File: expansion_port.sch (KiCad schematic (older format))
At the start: 2 parts

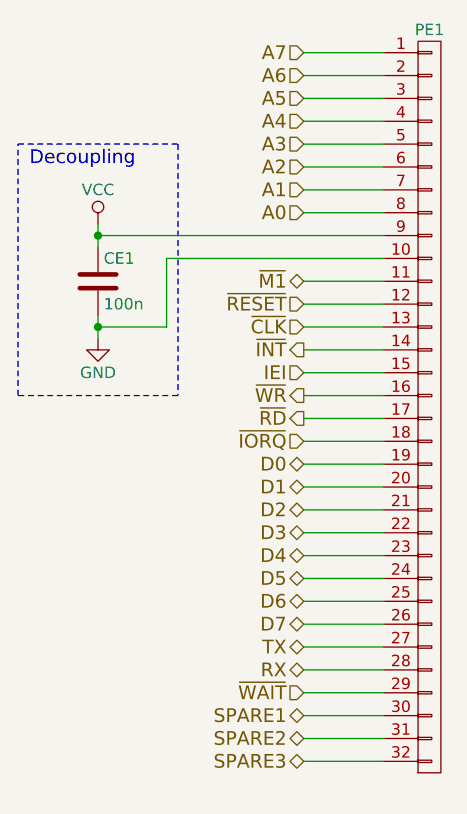
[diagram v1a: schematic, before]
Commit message: Added new expansion and GAL to layout.
Haven't routed the osc. or the reset.
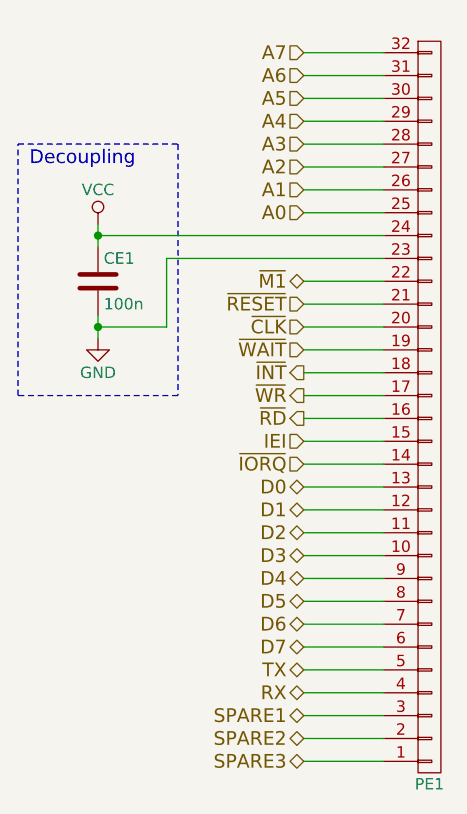
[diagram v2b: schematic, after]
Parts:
- PE1: footprint (none) -> Socket_Strips:Socket_Strip_Angled_1x32
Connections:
- net A0: now also PE1.25 (P25); no longer PE1.8 (P8)
- net A1: now also PE1.26 (P26); no longer PE1.7 (P7)
- net A2: now also PE1.27 (P27); no longer PE1.6 (P6)
- net A3: now also PE1.28 (P28); no longer PE1.5 (P5)
- net A4: now also PE1.29 (P29); no longer PE1.4 (P4)
- net A5: now also PE1.30 (P30); no longer PE1.3 (P3)
- net A6: now also PE1.31 (P31); no longer PE1.2 (P2)
- net A7: now also PE1.32 (P32); no longer PE1.1 (P1)
- net D0: now also PE1.13 (P13); no longer PE1.19 (P19)
- net D1: now also PE1.12 (P12); no longer PE1.20 (P20)
- net D2: now also PE1.11 (P11); no longer PE1.21 (P21)
- net D3: now also PE1.10 (P10); no longer PE1.22 (P22)
- net D4: now also PE1.9 (P9); no longer PE1.23 (P23)
- net D5: now also PE1.8 (P8); no longer PE1.24 (P24)
- net D6: now also PE1.7 (P7); no longer PE1.25 (P25)
- net D7: now also PE1.6 (P6); no longer PE1.26 (P26)
- net GND: now also PE1.23 (P23); no longer PE1.10 (P10)
- net RX: now also PE1.4 (P4); no longer PE1.28 (P28)
- net SPARE1: now also PE1.3 (P3); no longer PE1.30 (P30)
- net SPARE2: now also PE1.2 (P2); no longer PE1.31 (P31)
- net SPARE3: now also PE1.1 (P1); no longer PE1.32 (P32)
- net TX: now also PE1.5 (P5); no longer PE1.27 (P27)
- net VCC: now also PE1.24 (P24); no longer PE1.9 (P9)
- net ~CLK: now also PE1.20 (P20); no longer PE1.13 (P13)
- net ~INT: now also PE1.18 (P18); no longer PE1.14 (P14)
- net ~IORQ: now also PE1.14 (P14); no longer PE1.18 (P18)
- net ~M1: now also PE1.22 (P22); no longer PE1.11 (P11)
- net ~RD: now also PE1.16 (P16); no longer PE1.17 (P17)
- net ~RESET: now also PE1.21 (P21); no longer PE1.12 (P12)
- net ~WAIT: now also PE1.19 (P19); no longer PE1.29 (P29)
- net ~WR: now also PE1.17 (P17); no longer PE1.16 (P16)
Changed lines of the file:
@@
 Text HLabel 3500 2750 0    60   Input ~ 0
 A7
-Text HLabel 3500 4550 0    60   3State ~ 0
+Text HLabel 3500 4650 0    60   3State ~ 0
 D0
-Text HLabel 3500 4650 0    60   3State ~ 0
+Text HLabel 3500 4750 0    60   3State ~ 0
 D1
-Text HLabel 3500 4750 0    60   3State ~ 0
+Text HLabel 3500 4850 0    60   3State ~ 0
 D2
-Text HLabel 3500 4850 0    60   3State ~ 0
+Text HLabel 3500 4950 0    60   3State ~ 0
 D3
-Text HLabel 3500 4950 0    60   3State ~ 0
+Text HLabel 3500 5050 0    60   3State ~ 0
 D4
-Text HLabel 3500 5050 0    60   3State ~ 0
+Text HLabel 3500 5150 0    60   3State ~ 0
 D5
-Text HLabel 3500 5150 0    60   3State ~ 0
+Text HLabel 3500 5250 0    60   3State ~ 0
 D6
-Text HLabel 3500 5250 0    60   3State ~ 0
+Text HLabel 3500 5350 0    60   3State ~ 0
 D7
 Text HLabel 3500 3750 0    60   3State ~ 0
 ~M1
-Text HLabel 3500 4450 0    60   Input ~ 0
+Text HLabel 3500 4550 0    60   Input ~ 0
 ~IORQ
 Wire Wire Line
@@
 Text HLabel 3500 3950 0    60   Input ~ 0
 ~CLK
-Text HLabel 3500 4050 0    60   Output ~ 0
+Text HLabel 3500 4150 0    60   Output ~ 0
 ~INT
 Text HLabel 3500 4250 0    60   Output ~ 0
@@
 Text HLabel 3500 4350 0    60   Output ~ 0
 ~RD
-Text HLabel 3500 4150 0    60   Input ~ 0
+Text HLabel 3500 4450 0    60   Input ~ 0
 IEI
 Wire Wire Line
@@
 F 0 "PE1" H 4050 5950 50  0000 C CNN
 F 1 "CONN_01X32" V 4150 4300 50  0001 C CNN
-F 2 "" H 4050 4300 50  0000 C CNN
+F 2 "Socket_Strips:Socket_Strip_Angled_1x32" H 4050 4300 50  0001 C CNN
 F 3 "" H 4050 4300 50  0000 C CNN
 	1    4050 4300
-	1    0    0    -1
+	1    0    0    1
 $EndComp
 Wire Wire Line
@@
 Wire Wire Line
 	3500 5450 3850 5450
+Text HLabel 3500 5550 0    60   BiDi ~ 0
+RX
 Text HLabel 3500 5450 0    60   BiDi ~ 0
-RX
-Text HLabel 3500 5350 0    60   BiDi ~ 0
 TX
 Wire Wire Line
 	3500 4150 3850 4150
-Text HLabel 3500 5550 0    60   Input ~ 0
+Text HLabel 3500 4050 0    60   Input ~ 0
 ~WAIT
 Wire Wire Line
